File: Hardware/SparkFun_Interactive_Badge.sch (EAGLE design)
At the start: 33 parts, among them Q1 DMG2307L, U1 MIC5205-3.3V, U2 ATMEGA328P, U3 CY7C65213

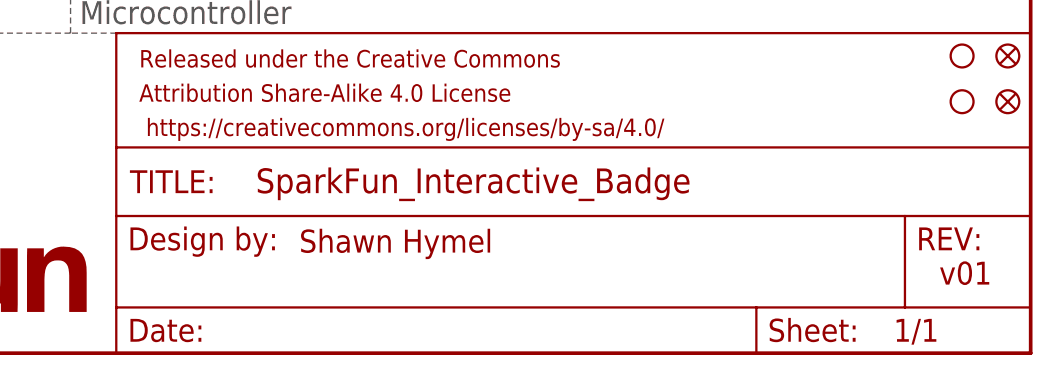
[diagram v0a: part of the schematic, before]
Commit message: Colored in silk for required headers.
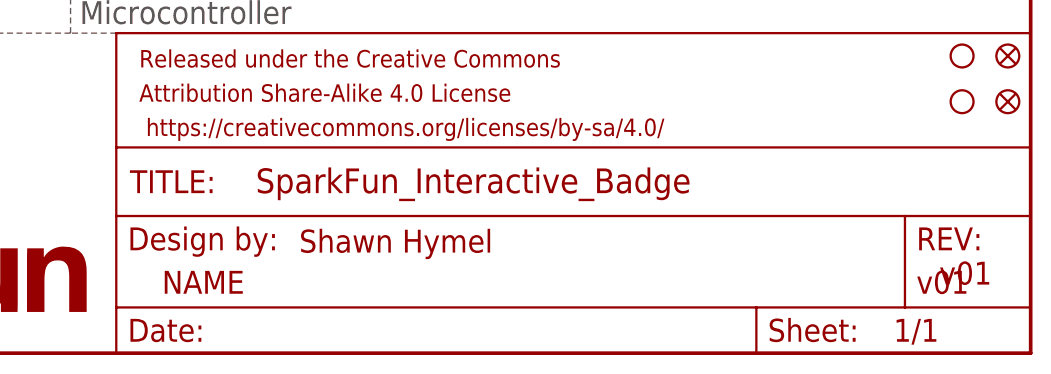
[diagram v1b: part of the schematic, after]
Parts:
- FRAME1: value FRAME-LETTER -> (none)
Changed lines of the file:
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@@
 <instances>
 <instance part="FRAME1" gate="G$1" x="0" y="0"/>
-<instance part="FRAME1" gate="G$2" x="147.32" y="0"/>
+<instance part="FRAME1" gate="V" x="147.32" y="0"/>
 <instance part="FID1" gate="G$1" x="246.38" y="33.02"/>
 <instance part="FID2" gate="G$1" x="246.38" y="27.94"/>

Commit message: Updated frame with name
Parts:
- FRAME1: DESIGNER (none) -> Shawn Hymel
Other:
- note removed: "Shawn Hymel"
- note removed: "v01"
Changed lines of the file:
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@@
 </classes>
 <parts>
-<part name="FRAME1" library="SparkFun-Aesthetics" deviceset="FRAME-LETTER" device=""/>
+<part name="FRAME1" library="SparkFun-Aesthetics" deviceset="FRAME-LETTER" device="">
+<attribute name="DESIGNER" value="Shawn Hymel"/>
+</part>
 <part name="FID1" library="SparkFun-Aesthetics" deviceset="FIDUCIAL" device="1X2"/>
 <part name="FID2" library="SparkFun-Aesthetics" deviceset="FIDUCIAL" device="1X2"/>
@@
 <sheet>
 <plain>
-<text x="238.76" y="7.62" size="2.54" layer="94">v01</text>
-<text x="167.64" y="11.176" size="2.54" layer="94">Shawn Hymel</text>
 <text x="78.74" y="71.12" size="1.778" layer="97" align="center-right">RX (Pin 10)</text>
 <text x="78.74" y="66.04" size="1.778" layer="97" align="center-right">TX (Pin 11)</text>

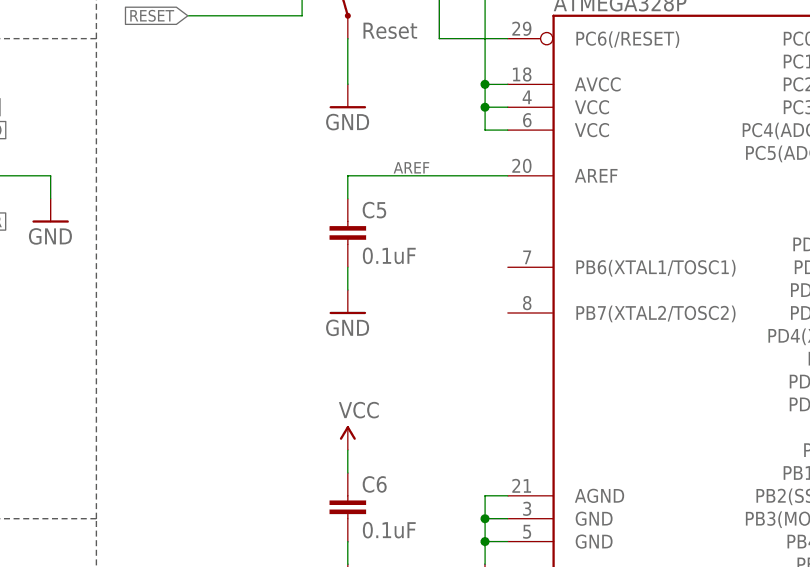
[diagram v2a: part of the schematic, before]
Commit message: Added 4MHz resonator.
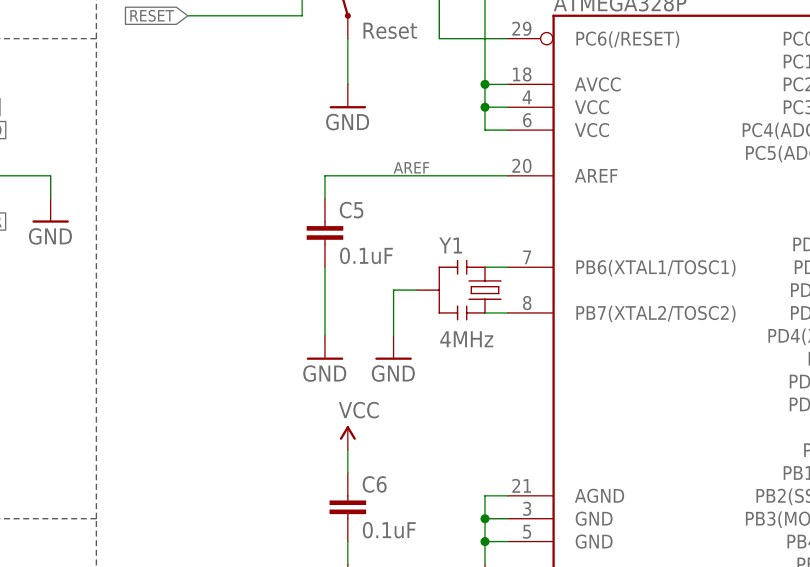
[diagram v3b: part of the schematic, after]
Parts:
- added Y1: 4MHz, SparkFun-FreqCtrl:RESONATOR4MHZ
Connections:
- new net N$5: U2.PB6(XTAL1/TOSC1), Y1.1
- new net N$6: U2.PB7(XTAL2/TOSC2), Y1.3
- net GND: now also Y1.2
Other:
- moved on the sheet: C5
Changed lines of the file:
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@@
 <setting verticaltext="up"/>
 </settings>
-<grid distance="0.1" unitdist="inch" unit="inch" style="lines" multiple="1" display="no" altdistance="0.01" altunitdist="inch" altunit="inch"/>
+<grid distance="0.1" unitdist="inch" unit="inch" style="lines" multiple="1" display="yes" altdistance="0.01" altunitdist="inch" altunit="inch"/>
 <layers>
 <layer number="1" name="Top" color="4" fill="1" visible="no" active="no"/>
@@
 <part name="JP4" library="SparkFun-Connectors" deviceset="M15" device="LOCK_NO_SILK" value="M15LOCK_NO_SILK"/>
 <part name="JP3" library="SparkFun-Connectors" deviceset="M15" device="LOCK_NO_SILK"/>
+<part name="Y1" library="SparkFun-FreqCtrl" deviceset="RESONATOR" device="4MHZ" value="4MHz"/>
+<part name="GND1" library="SparkFun-Aesthetics" deviceset="GND" device=""/>
 </parts>
 <sheets>
@@
 <instance part="SUPPLY6" gate="G$1" x="167.64" y="162.56"/>
 <instance part="SUPPLY7" gate="G$1" x="185.42" y="139.7"/>
-<instance part="C5" gate="G$1" x="170.18" y="111.76"/>
+<instance part="C5" gate="G$1" x="167.64" y="111.76"/>
 <instance part="GND8" gate="1" x="170.18" y="127"/>
-<instance part="GND9" gate="1" x="170.18" y="104.14"/>
+<instance part="GND9" gate="1" x="167.64" y="99.06"/>
 <instance part="GND10" gate="1" x="185.42" y="73.66"/>
 <instance part="C6" gate="G$1" x="170.18" y="81.28"/>
@@
 <instance part="JP4" gate="G$1" x="55.88" y="55.88" rot="R180"/>
 <instance part="JP3" gate="G$1" x="7.62" y="55.88"/>
+<instance part="Y1" gate="G$1" x="185.42" y="106.68" smashed="yes" rot="R270">
+<attribute name="NAME" x="180.34" y="110.744" size="1.778" layer="95"/>
+<attribute name="VALUE" x="180.34" y="100.33" size="1.778" layer="96"/>
+</instance>
+<instance part="GND1" gate="1" x="175.26" y="99.06"/>
 </instances>
 <busses>
@@
 <pinref part="C5" gate="G$1" pin="2"/>
 <pinref part="GND9" gate="1" pin="GND"/>
-<wire x1="170.18" y1="109.22" x2="170.18" y2="106.68" width="0.1524" layer="91"/>
+<wire x1="167.64" y1="109.22" x2="167.64" y2="101.6" width="0.1524" layer="91"/>
 </segment>
 <segment>
@@
 <label x="20.32" y="71.12" size="1.27" layer="95" xref="yes"/>
 </segment>
+<segment>
+<pinref part="Y1" gate="G$1" pin="2"/>
+<wire x1="177.8" y1="106.68" x2="175.26" y2="106.68" width="0.1524" layer="91"/>
+<wire x1="175.26" y1="106.68" x2="175.26" y2="101.6" width="0.1524" layer="91"/>
+<pinref part="GND1" gate="1" pin="GND"/>
+</segment>
 </net>
 <net name="VBAT" class="0">
@@
 <segment>
 <pinref part="U2" gate="G$1" pin="AREF"/>
-<wire x1="187.96" y1="119.38" x2="170.18" y2="119.38" width="0.1524" layer="91"/>
+<wire x1="187.96" y1="119.38" x2="167.64" y2="119.38" width="0.1524" layer="91"/>
 <pinref part="C5" gate="G$1" pin="1"/>
-<wire x1="170.18" y1="119.38" x2="170.18" y2="116.84" width="0.1524" layer="91"/>
+<wire x1="167.64" y1="119.38" x2="167.64" y2="116.84" width="0.1524" layer="91"/>
 <label x="175.26" y="119.634" size="1.27" layer="95"/>
 </segment>
@@
 </segment>
 </net>
+<net name="N$5" class="0">
+<segment>
+<pinref part="U2" gate="G$1" pin="PB6(XTAL1/TOSC1)"/>
+<pinref part="Y1" gate="G$1" pin="1"/>
+<wire x1="187.96" y1="109.22" x2="185.42" y2="109.22" width="0.1524" layer="91"/>
+</segment>
+</net>
+<net name="N$6" class="0">
+<segment>
+<pinref part="U2" gate="G$1" pin="PB7(XTAL2/TOSC2)"/>
+<pinref part="Y1" gate="G$1" pin="3"/>
+<wire x1="187.96" y1="104.14" x2="185.42" y2="104.14" width="0.1524" layer="91"/>
+</segment>
+</net>

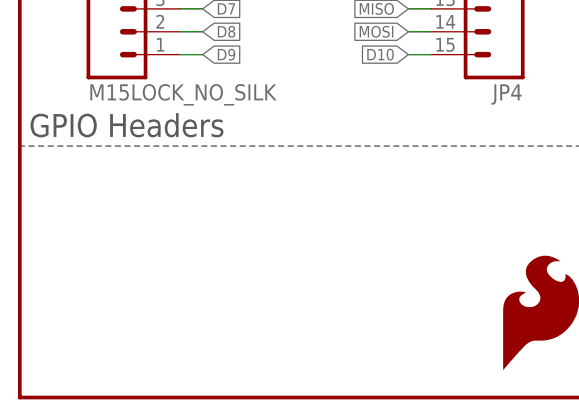
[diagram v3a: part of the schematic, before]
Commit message: Added badger logo.
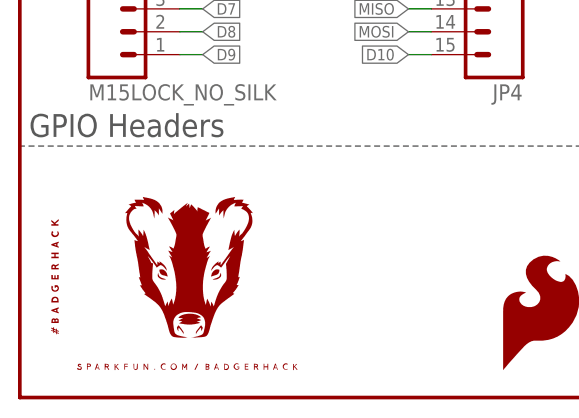
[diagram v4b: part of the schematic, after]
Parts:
- added U$2: BADGERHACK_LOGODUMMY, SparkFun-Aesthetics:BADGERHACK_LOGODUMMY
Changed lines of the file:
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@@
 <setting verticaltext="up"/>
 </settings>
-<grid distance="0.1" unitdist="inch" unit="inch" style="lines" multiple="1" display="yes" altdistance="0.01" altunitdist="inch" altunit="inch"/>
+<grid distance="0.1" unitdist="inch" unit="inch" style="lines" multiple="1" display="no" altdistance="0.01" altunitdist="inch" altunit="inch"/>
 <layers>
 <layer number="1" name="Top" color="4" fill="1" visible="no" active="no"/>
@@
 <part name="Y1" library="SparkFun-FreqCtrl" deviceset="RESONATOR" device="4MHZ" value="4MHz"/>
 <part name="GND1" library="SparkFun-Aesthetics" deviceset="GND" device=""/>
+<part name="U$2" library="SparkFun-Aesthetics" deviceset="BADGERHACK_LOGO" device="DUMMY"/>
 </parts>
 <sheets>
@@
 </instance>
 <instance part="GND1" gate="1" x="175.26" y="99.06"/>
+<instance part="U$2" gate="G$1" x="2.54" y="2.54"/>
 </instances>
 <busses>
